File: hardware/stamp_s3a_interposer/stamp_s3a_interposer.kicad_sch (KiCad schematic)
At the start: 0 parts

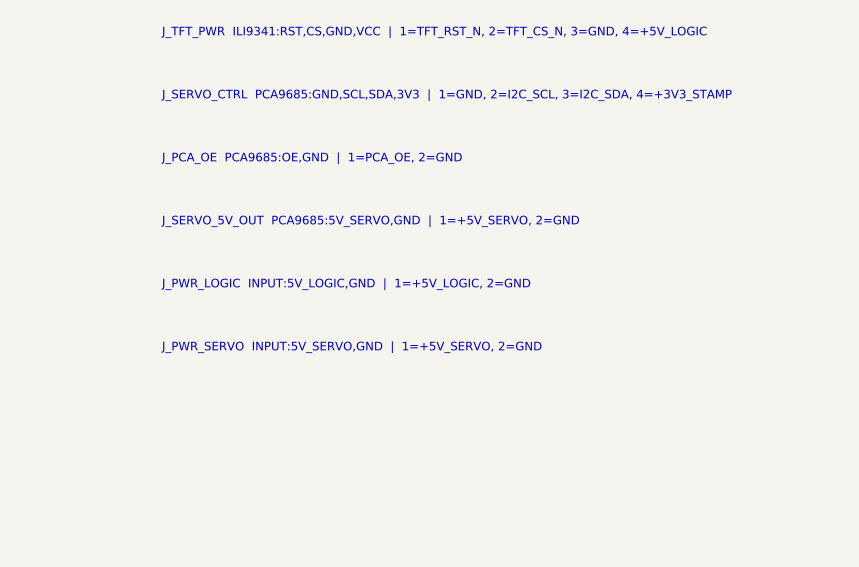
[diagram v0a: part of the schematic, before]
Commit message: Finalize compact Stamp-S3A interposer manufacturing files
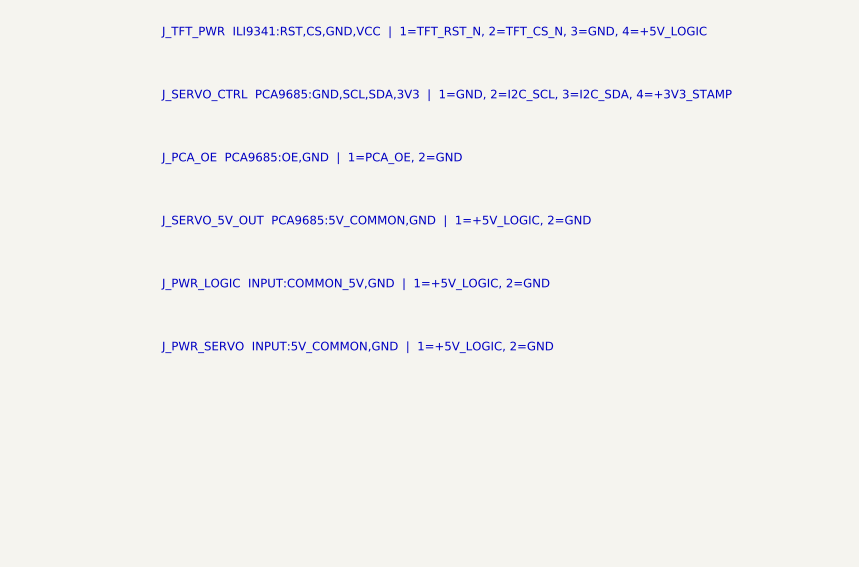
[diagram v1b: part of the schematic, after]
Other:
- note added: "J_PWR_LOGIC INPUT:COMMON_5V,GND | 1=+5V_LOGIC, 2=GND"
- note added: "J_PWR_SERVO INPUT:5V_COMMON,GND | 1=+5V_LOGIC, 2=GND"
- note added: "J_SERVO_5V_OUT PCA9685:5V_COMMON,GND | 1=+5V_LOGIC, 2=GND"
- note removed: "J_PWR_LOGIC INPUT:5V_LOGIC,GND | 1=+5V_LOGIC, 2=GND"
- note removed: "J_PWR_SERVO INPUT:5V_SERVO,GND | 1=+5V_SERVO, 2=GND"
- note removed: "J_SERVO_5V_OUT PCA9685:5V_SERVO,GND | 1=+5V_SERVO, 2=GND"
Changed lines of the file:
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@@
     (effects (font (size 0.95 0.95)) (justify left bottom))
   )
-  (text "J_SERVO_5V_OUT  PCA9685:5V_SERVO,GND  |  1=+5V_SERVO, 2=GND"
+  (text "J_SERVO_5V_OUT  PCA9685:5V_COMMON,GND  |  1=+5V_LOGIC, 2=GND"
     (exclude_from_sim no)
     (at 148.00 76.00 0)
     (effects (font (size 0.95 0.95)) (justify left bottom))
   )
-  (text "J_PWR_LOGIC  INPUT:5V_LOGIC,GND  |  1=+5V_LOGIC, 2=GND"
+  (text "J_PWR_LOGIC  INPUT:COMMON_5V,GND  |  1=+5V_LOGIC, 2=GND"
     (exclude_from_sim no)
     (at 148.00 83.00 0)
     (effects (font (size 0.95 0.95)) (justify left bottom))
   )
-  (text "J_PWR_SERVO  INPUT:5V_SERVO,GND  |  1=+5V_SERVO, 2=GND"
+  (text "J_PWR_SERVO  INPUT:5V_COMMON,GND  |  1=+5V_LOGIC, 2=GND"
     (exclude_from_sim no)
     (at 148.00 90.00 0)
